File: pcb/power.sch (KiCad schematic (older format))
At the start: 70 parts, among them SW1 SW_SP3T, U1 LTC3456, U100 MCIMX7S5EVM08SC, U2 LTC3549, U3 LTC3549

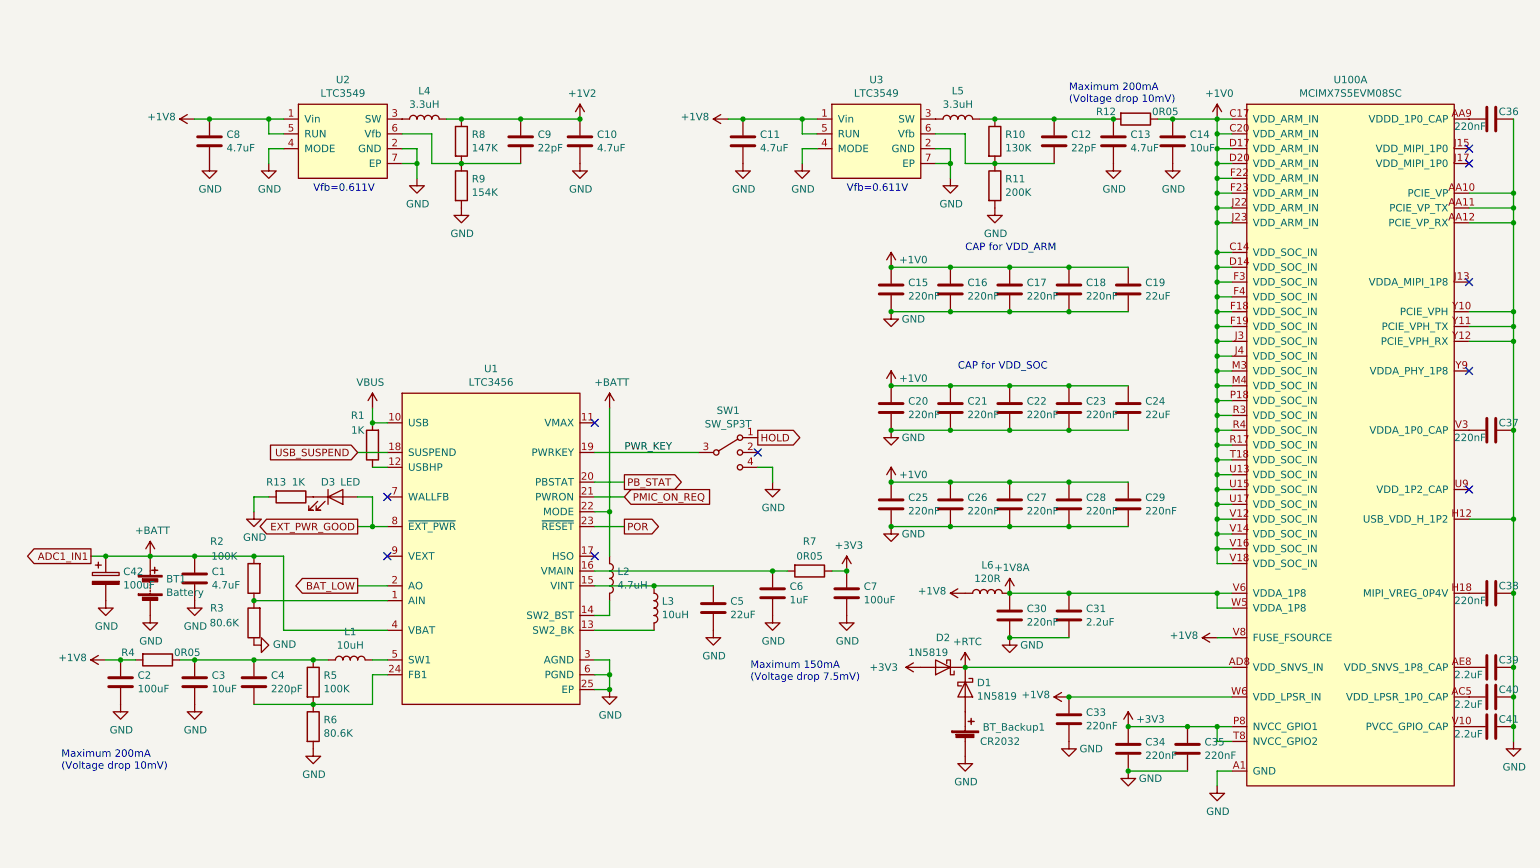
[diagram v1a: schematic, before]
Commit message: pcb: move cpu power to power page
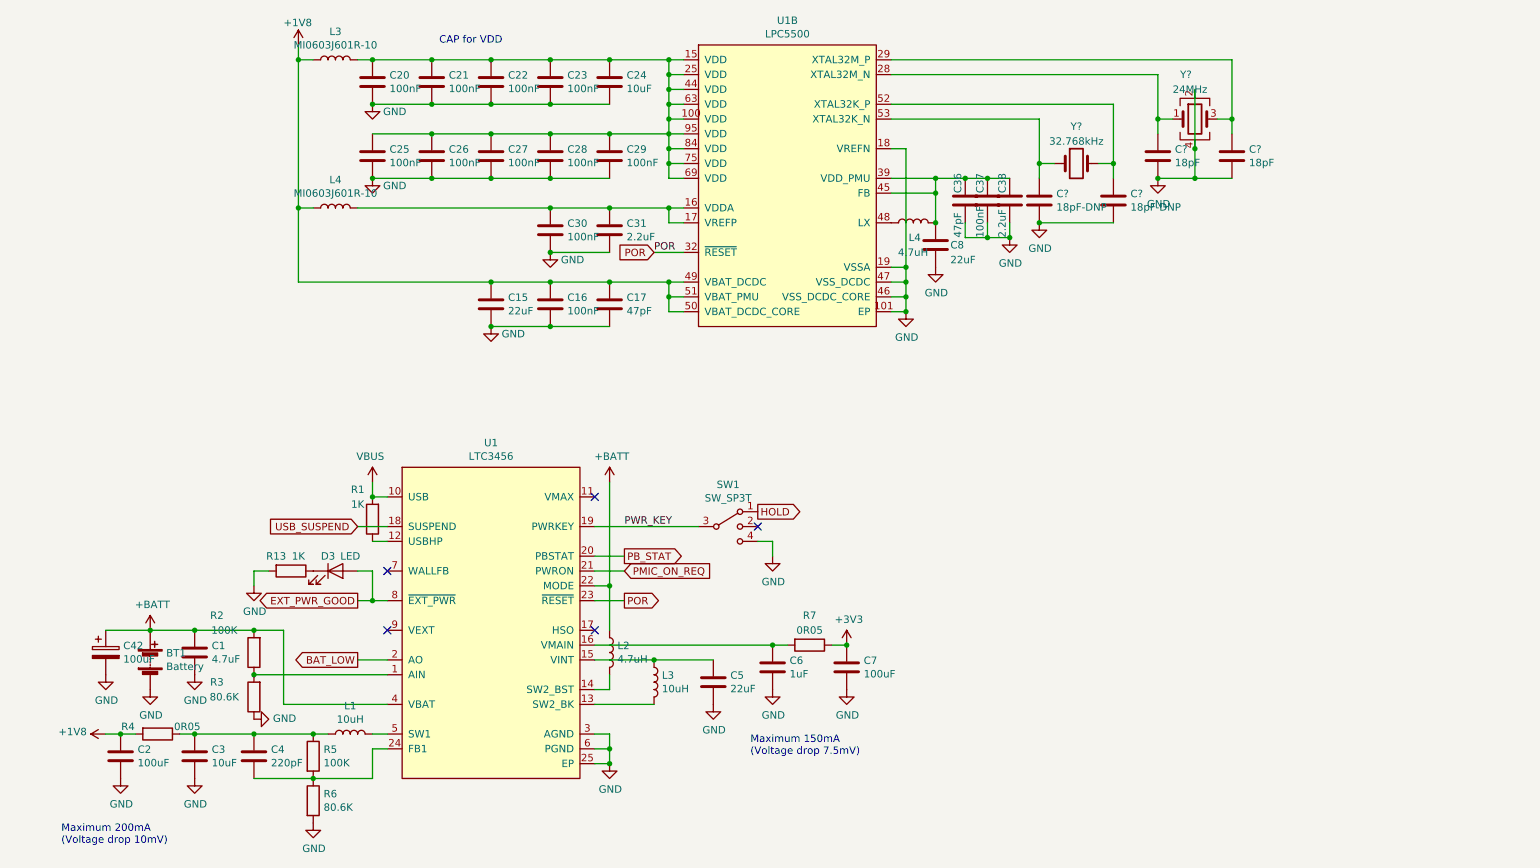
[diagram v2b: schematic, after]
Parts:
- removed BT_Backup1: CR2032, footprints:BatteryHolder_CR1220, symbol Device:Battery_Cell
- removed C10, C11, C13: 4.7uF, Capacitor_SMD:C_0603_1608Metric, symbol Device:C
- removed C12, C9: 22pF, Capacitor_SMD:C_0402_1005Metric, symbol Device:C
- removed C14: 10uF, Capacitor_SMD:C_0603_1608Metric, symbol Device:C
- removed C18, C33, C34, C35: 220nF, Capacitor_SMD:C_0402_1005Metric, symbol Device:C
- removed C19: 22uF, Capacitor_SMD:C_0603_1608Metric, symbol Device:C
- removed C39, C40, C41: 2.2uF, Capacitor_SMD:C_0402_1005Metric, symbol Device:C
- removed D1, D2: 1N5819, Diode_SMD:D_SOD-123, symbol Device:D_Schottky
- removed L4, L5: 3.3uH, Inductor_SMD:L_Vishay_IHLP-1212, symbol Device:L
- removed L6: 120R, Inductor_SMD:L_0402_1005Metric, symbol Device:L
- removed R10: 130K, Resistor_SMD:R_0603_1608Metric, symbol Device:R
- removed R11: 200K, Resistor_SMD:R_0603_1608Metric, symbol Device:R
- removed R12: 0R05, Resistor_SMD:R_1206_3216Metric, symbol Device:R
- removed R8: 147K, Resistor_SMD:R_0603_1608Metric, symbol Device:R
- removed R9: 154K, Resistor_SMD:R_0603_1608Metric, symbol Device:R
- removed U100: MCIMX7S5EVM08SC, footprints:BGA-541_25x25_19.0x19.0mm, symbol symbols:MCIMX7S5EVM08SC
- removed U2, U3: LTC3549, Package_DFN_QFN:DFN-6-1EP_3x2mm_P0.5mm_EP1.65x1.35mm, symbol symbols:LTC3549
- added C? (x2): 18pF-DNP, Capacitor_SMD:C_0402_1005Metric, symbol Device:C
- added C? (x2): 18pF, Capacitor_SMD:C_0402_1005Metric, symbol Device:C
- added L3, L4: MI0603J601R-10, Inductor_SMD:L_0402_1005Metric, symbol Device:L
- added L4: 4.7uH, Inductor_SMD:L_Vishay_IHLP-1212, symbol Device:L
- added unit 2 of U1
- added Y?: 32.768kHz, Crystal:Crystal_SMD_TXC_9HT11-2Pin_2.0x1.2mm_HandSoldering, symbol Device:Crystal
- added Y?: 24MHz, Oscillator:Oscillator_SMD_Abracon_ASE-4Pin_3.2x2.5mm, symbol Device:Crystal_GND24
- C15: value 220nF -> 22uF; footprint Capacitor_SMD:C_0402_1005Metric -> Capacitor_SMD:C_0603_1608Metric
- C16, C20, C21, C22, C23, C25, C26, C27, C28, C29, C30, C37: value 220nF -> 100nF
- C17, C36: value 220nF -> 47pF
- C24: value 22uF -> 10uF
- C38: value 220nF -> 2.2uF
- C8: value 4.7uF -> 22uF
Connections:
- net +1V8: now also C15.1, C16.1, C17.1, L3.1, L4.1, U1.49 (VBAT_DCDC), U1.50 (VBAT_DCDC_CORE), U1.51 (VBAT_PMU); no longer C8.1
- net GND: now also C36.2, C37.2, C38.2, C?.2, C?.2, C?.2, C?.2, U1.101 (EP), U1.18 (VREFN), U1.19 (VSSA), U1.46 (VSS_DCDC_CORE), U1.47 (VSS_DCDC), Y?.2, Y?.4; no longer C36.1, C37.1, C38.1
- net POR: now also U1.32 (~RESET)
- net +1V0: no longer names the net of C20.1, C21.1, C22.1, C23.1, C24.1, C25.1, C26.1, C27.1, C28.1, C29.1
- net +1V0: now also L3.2, U1.100 (VDD), U1.15 (VDD), U1.25 (VDD), U1.44 (VDD), U1.63 (VDD), U1.69 (VDD), U1.75 (VDD), U1.84 (VDD), U1.95 (VDD); no longer C15.1, C16.1, C17.1
- net +1V8A: no longer names the net of C30.1, C31.1
- net +1V8A: now also L4.2, U1.16 (VDDA), U1.17 (VREFP)
- new net: C?.1, U1.53 (XTAL32K_N), Y?.1
- new net: C?.1, U1.52 (XTAL32K_P), Y?.2
- new net: C?.1, U1.28 (XTAL32M_N), Y?.1
- new net: C?.1, U1.29 (XTAL32M_P), Y?.3
- new net: C36.1, C37.1, C38.1, C8.1, L4.2, U1.39 (VDD_PMU), U1.45 (FB)
- new net: L4.1, U1.48 (LX)
- no-connect marks 10 -> 5
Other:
- note added: "CAP for VDD"
- note removed: "CAP for VDD_ARM"
- note removed: "CAP for VDD_SOC"
- note removed: "Vfb=0.611V"
- moved on the sheet: BT1, C1, C15, C16, C17, C2, C20, C21, C22, C23, C24, C25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

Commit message: pcb: rev 0.1
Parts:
- removed C? (x2): 18pF-DNP, Capacitor_SMD:C_0402_1005Metric, symbol Device:C
- removed D3: LED, LED_THT:LED_D5.0mm, symbol Device:LED
- removed R13: 1K, Resistor_SMD:R_0603_1608Metric, symbol Device:R
- L5: renamed from L3; footprint Inductor_SMD:L_0402_1005Metric -> Inductor_SMD:L_0603_1608Metric
- L6: renamed from L4; footprint Inductor_SMD:L_0402_1005Metric -> Inductor_SMD:L_0603_1608Metric
- gave numbers to parts that had none: 4
- renumbered U1 to U100
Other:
- moved on the sheet: BT1, C1, C2, C3, C4, C42, C5, C6, C7, L1, L2, L3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

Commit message: pcb: fixing i2c numbering; add filtering for lcd
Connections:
- net +1V8: no longer C15.1, C16.1, C17.1, L5.1, L6.1, U100.49 (VBAT_DCDC), U100.50 (VBAT_DCDC_CORE), U100.51 (VBAT_PMU)
- net +3V3: now also C15.1, C16.1, C17.1, L5.1, L6.1, U100.49 (VBAT_DCDC), U100.50 (VBAT_DCDC_CORE), U100.51 (VBAT_PMU)
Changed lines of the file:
@@
 	6900 2100 6600 2100
-$Comp
-L power:+1V8 #PWR0106
-U 1 1 5D90AAF6
-P 2600 1200
-F 0 "#PWR0106" H 2600 1050 50  0001 C CNN
-F 1 "+1V8" H 2500 1350 50  0000 L CNN
-F 2 "" H 2600 1200 50  0001 C CNN
-F 3 "" H 2600 1200 50  0001 C CNN
-	1    2600 1200
-	1    0    0    -1
-$EndComp
 $Comp
 L Device:L L5
@@
 Wire Wire Line
 	5000 4650 5200 4650
+$Comp
+L power:+3V3 #PWR0109
+U 1 1 5DBC7126
+P 2600 1200
+F 0 "#PWR0109" H 2600 1050 50  0001 C CNN
+F 1 "+3V3" H 2615 1373 50  0000 C CNN
+F 2 "" H 2600 1200 50  0001 C CNN
+F 3 "" H 2600 1200 50  0001 C CNN
+	1    2600 1200
+	1    0    0    -1
+$EndComp
 $EndSCHEMATC
